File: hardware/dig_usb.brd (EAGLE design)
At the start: 146.1 x 102.6 mm, 172 parts, among them IC1 AT90USB1287-AU, IC202 DS1337S, IC203 MAX487CSA, IC204 74HC166D, IC301 LTV-356T, IC302 LTV-356T, IC303 LTV-356T, IC304 LTV-356T, IC305 LTV-356T, IC306 LTV-356T, IC307 LTV-356T, IC308 LTV-356T, K401 S202S02, K402 S202S02, K403 S202S02, K404 S202S02, K405 S202S02, K406 S202S02, K407 S202S02, K408 S202S02, Q1 16MHz, Q201 32,768kHz, T301 BCR191, T302 BCR191, T303 BCR191, T304 BCR191, T305 BCR191, T306 BCR191, T307 BCR191, T308 BCR191, X101 RIA-73-02, X201 ISP, X202 RIA-73-02, X301 RIA-73-02, X302 RIA-73-02, X303 RIA-73-02, X304 RIA-73-02, X305 RIA-73-02, X401 RIA-73-02, X402 RIA-73-02, X403 RIA-73-02, X404 RIA-73-02, X405 RIA-73-02

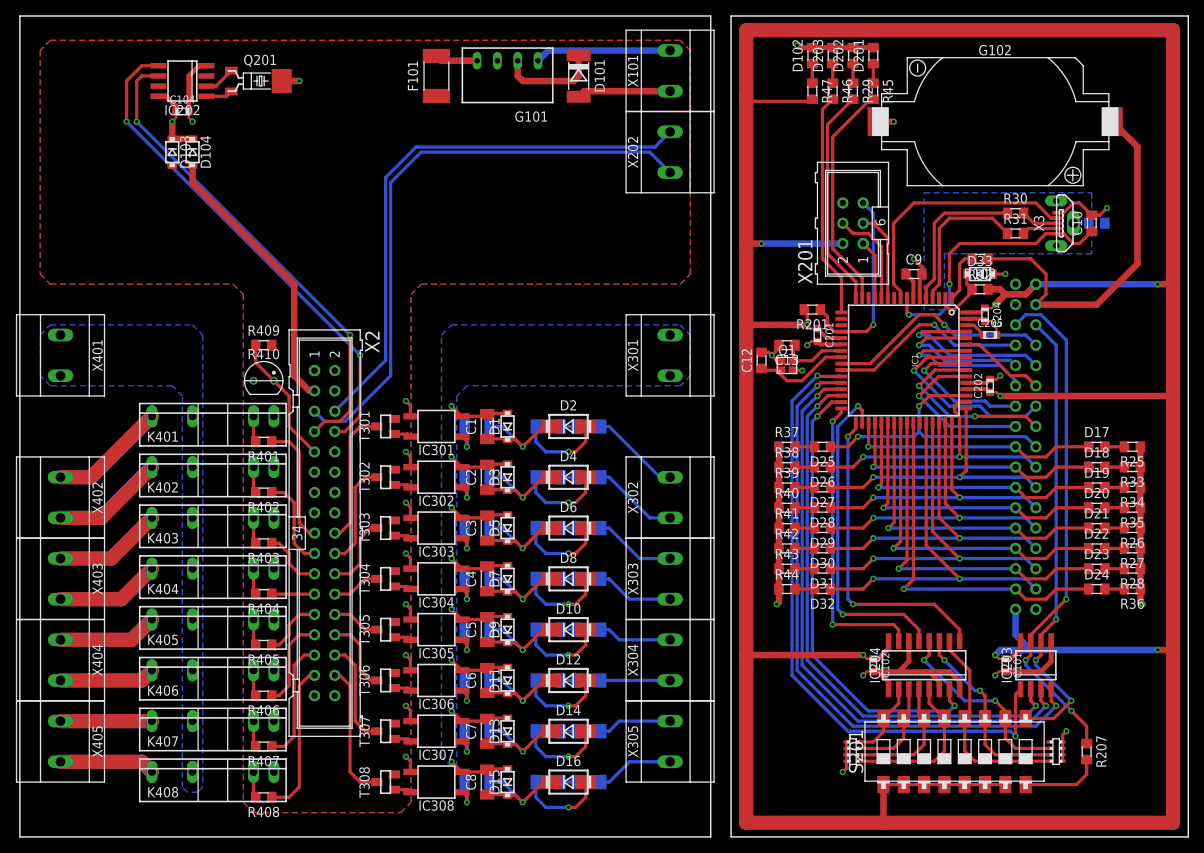
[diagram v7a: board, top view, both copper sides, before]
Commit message: CHIP Gehäusebauformen ausgetauscht
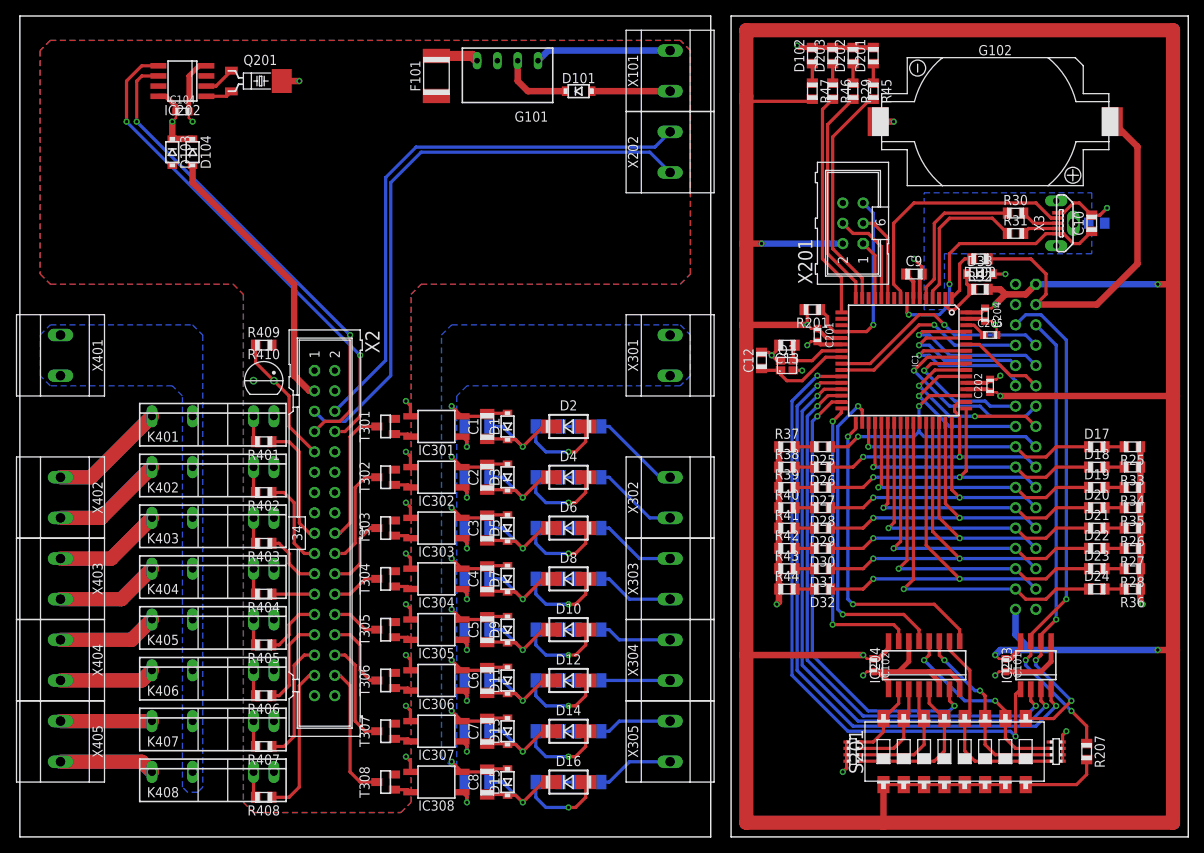
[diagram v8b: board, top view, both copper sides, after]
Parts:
- D101: value LL5819 -> SD103; device diode:MELF -> diode:SOD123
- moved D101 1.91 mm to (69.8, 92.7), turned to 0 degrees
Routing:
- net N$23: track 12.7 -> 9.04 mm
- net N$24: track 11.7 -> 9.78 mm
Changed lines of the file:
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@@
 <wire x1="80.01" y1="8.89" x2="82.55" y2="8.89" width="0" layer="51"/>
 <wire x1="80.01" y1="3.81" x2="82.55" y2="3.81" width="0" layer="51"/>
-<rectangle x1="0" y1="-0.508" x2="86.36" y2="2.54" layer="42"/>
-<rectangle x1="0" y1="99.06" x2="86.36" y2="102.108" layer="42"/>
+<rectangle x1="0" y1="-0.508" x2="86.36" y2="2.54" layer="40"/>
+<rectangle x1="0" y1="99.06" x2="86.36" y2="102.108" layer="40"/>
 <rectangle x1="12.7" y1="-0.508" x2="13.97" y2="102.108" layer="39"/>
 <rectangle x1="72.39" y1="-0.508" x2="73.66" y2="102.108" layer="39"/>
@@
 <attribute name="OC_FARNELL" value="1007547" x="-3.81" y="132.08" size="1.778" layer="27" rot="R180" display="off"/>
 </element>
-<element name="D101" library="diode" package="MELF" value="LL5819" x="69.85" y="94.615" rot="R270"/>
+<element name="D101" library="diode" package="SOD123" value="SD103" x="69.85" y="92.71"/>
 <element name="D102" library="led" package="CHIP_0805" value="GN" x="99.06" y="97.155" rot="R90"/>
 <element name="F101" library="sicherung" package="CHIP_1812" value="194600-020" x="52.07" y="94.615" rot="R90"/>
@@
 <contactref element="G101" pad="2"/>
 <contactref element="D101" pad="K"/>
-<wire x1="62.23" y1="96.52" x2="62.23" y2="94.615" width="0.8128" layer="1"/>
-<wire x1="62.23" y1="94.615" x2="62.865" y2="93.98" width="0.8128" layer="1"/>
-<wire x1="62.865" y1="93.98" x2="69.215" y2="93.98" width="0.8128" layer="1"/>
-<wire x1="69.215" y1="93.98" x2="69.85" y2="94.615" width="0.8128" layer="1"/>
-<wire x1="69.85" y1="94.615" x2="69.85" y2="97.215" width="0.8128" layer="1"/>
+<wire x1="62.23" y1="96.52" x2="62.23" y2="93.98" width="0.8128" layer="1"/>
+<wire x1="62.23" y1="93.98" x2="63.5" y2="92.71" width="0.8128" layer="1"/>
+<wire x1="63.5" y1="92.71" x2="68.2" y2="92.71" width="0.8128" layer="1"/>
 </signal>
 <signal name="N$24">
 <contactref element="D101" pad="A"/>
 <contactref element="X101" pad="1"/>
-<wire x1="69.85" y1="92.015" x2="70.545" y2="92.71" width="0.8128" layer="1"/>
-<wire x1="70.545" y1="92.71" x2="81.28" y2="92.71" width="0.8128" layer="1"/>
+<wire x1="81.28" y1="92.71" x2="71.5" y2="92.71" width="0.8128" layer="1"/>
 </signal>
 <signal name="N$41">
 <contactref element="G101" pad="4"/>
 <contactref element="F101" pad="2"/>
-<wire x1="52.07" y1="97.115" x2="52.665" y2="96.52" width="0.8128" layer="1"/>
-<wire x1="52.665" y1="96.52" x2="57.15" y2="96.52" width="0.8128" layer="1"/>
+<wire x1="52.07" y1="97.115" x2="56.555" y2="97.115" width="1.27" layer="1"/>
+<wire x1="56.555" y1="97.115" x2="57.15" y2="96.52" width="1.27" layer="1"/>
 </signal>
 <signal name="N$64">
